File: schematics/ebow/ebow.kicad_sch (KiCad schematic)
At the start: 11 parts, among them U1 LM386

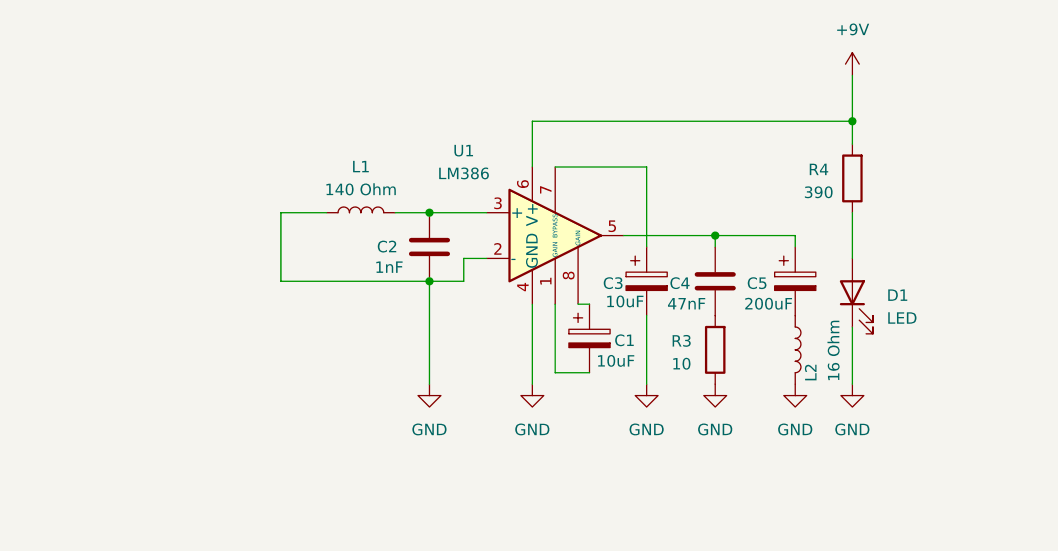
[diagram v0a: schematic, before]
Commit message: fixed ebow schematic
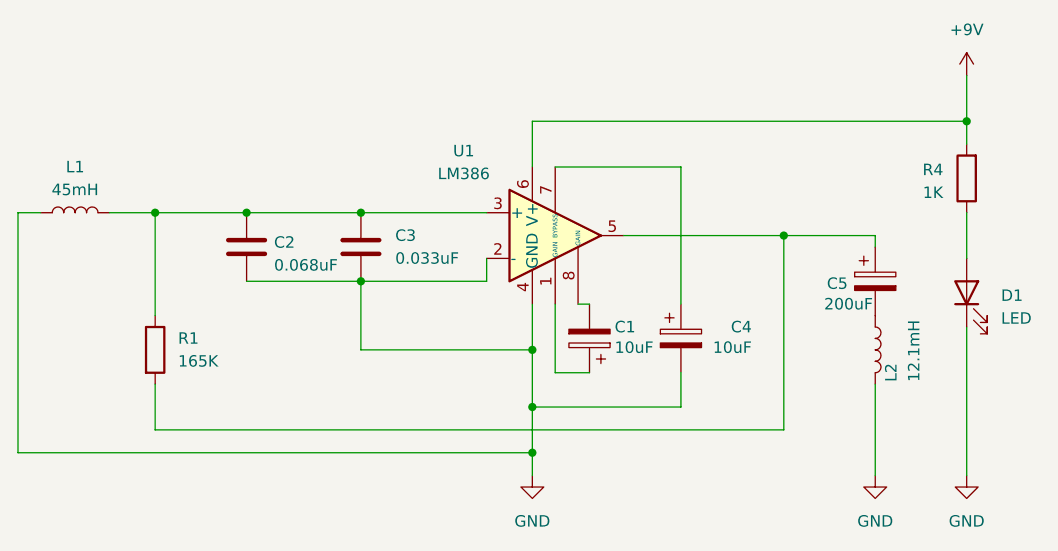
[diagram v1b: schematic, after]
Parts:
- removed C3: 10uF, symbol Device:C_Polarized
- removed C4: 47nF, symbol Device:C
- removed R3: 10, symbol Device:R
- added C3: 0.033uF, symbol Device:C
- added C4: 10uF, symbol Device:C_Polarized
- added R1: 165K, symbol Device:R
- C2: value 1nF -> 0.068uF
- L1: value 140 Ohm -> 45mH
- L2: value 16 Ohm -> 12.1mH
- R4: value 390 -> 1K
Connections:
- net GND: now also C3.2, C4.2
- net at C5.1, U1.5: now also R1.2
- net at C1.1: now also U1.1 (GAIN); no longer U1.8 (GAIN)
- net at C1.2: now also U1.8 (GAIN); no longer U1.1 (GAIN)
- net at C2.1, L1.2, U1.3 (+): now also C3.1, R1.1
- net at U1.7 (BYPASS): now also C4.1
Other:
- moved on the sheet: C1, C5, D1, L1, L2, R4
